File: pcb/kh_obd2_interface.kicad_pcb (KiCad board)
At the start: 2 copper layers, 19 parts, among them J1 OBD2, Q1 CSD18540Q5B, U1 LM74500-Q1, U2 TVS2700DRV, U3 TPSM33620S5QRDNRQ1

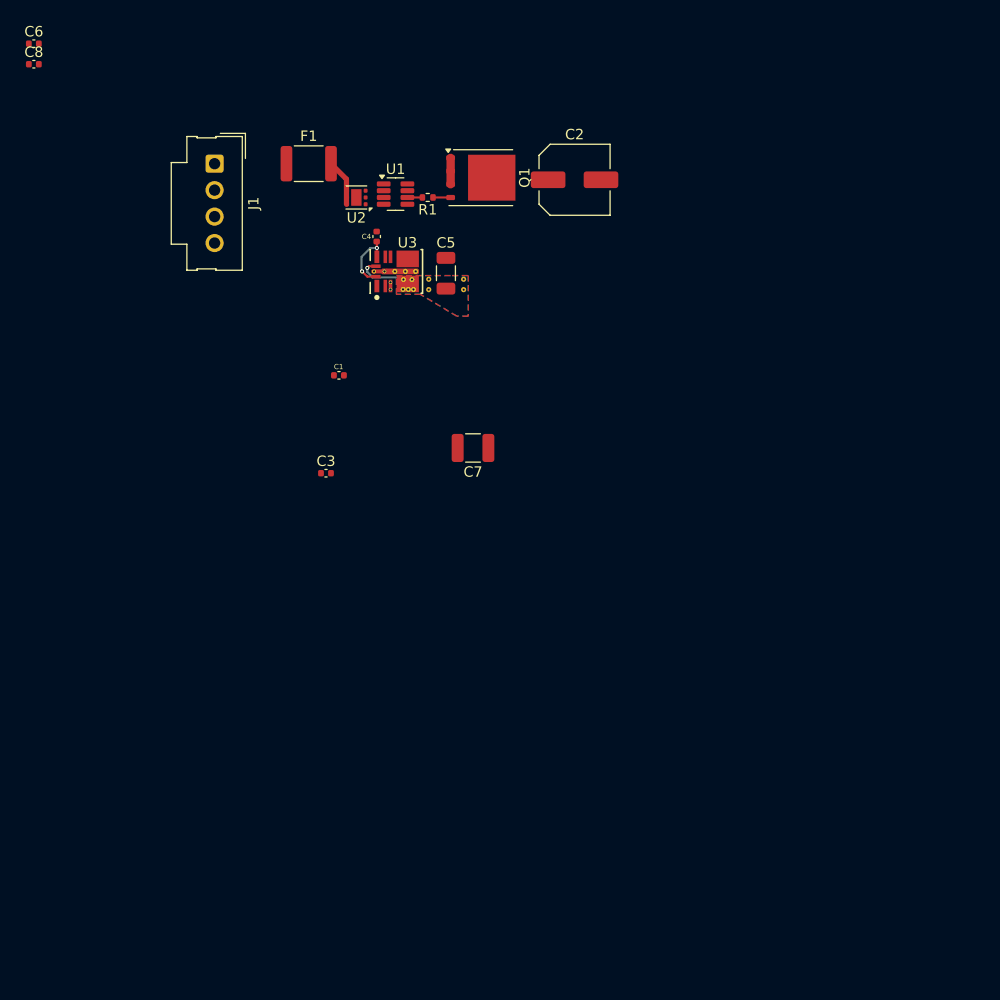
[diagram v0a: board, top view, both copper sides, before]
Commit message: delete old files, fix buck footprint, routing
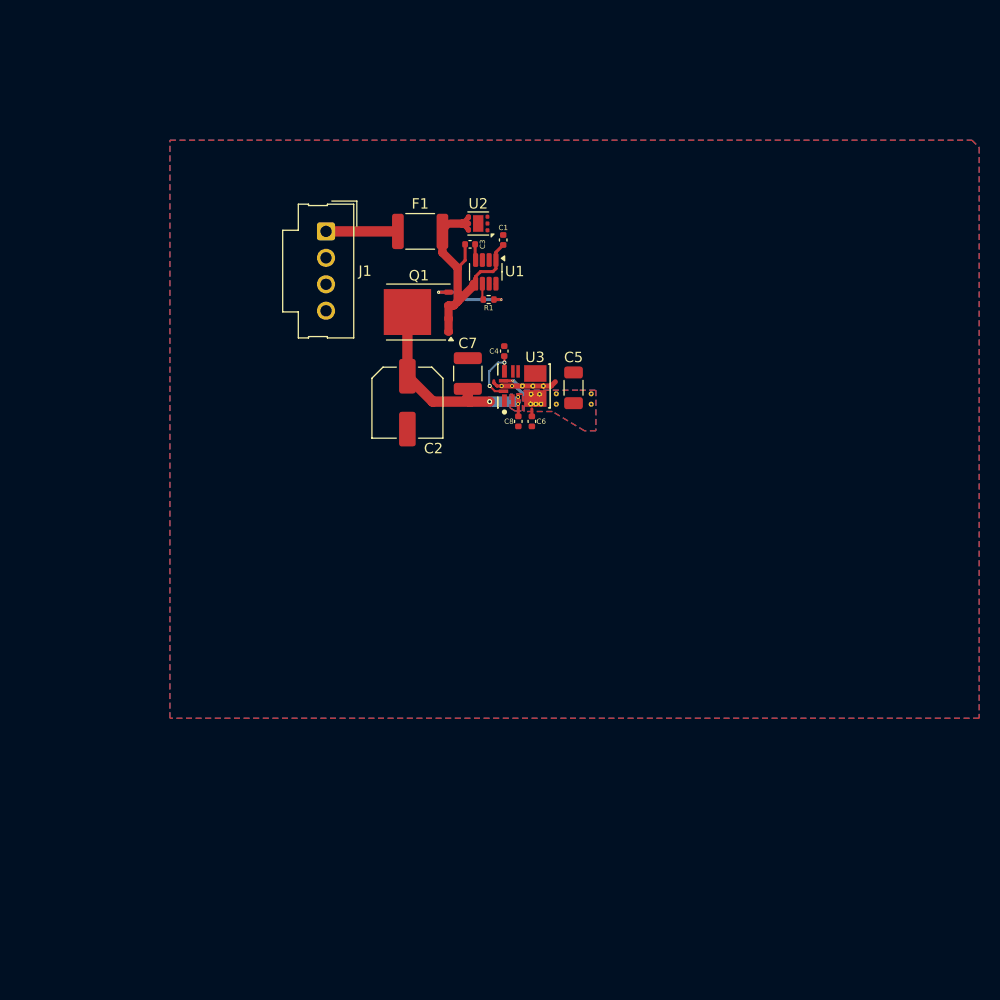
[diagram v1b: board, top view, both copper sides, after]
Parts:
- moved C6 60.0 mm to (48.8, 41.0), turned to 90 degrees
- moved C8 57.8 mm to (47.5, 41.0), turned to 90 degrees
- moved C2 26.8 mm to (36.8, 39.2), turned to -90 degrees
- moved C3 26.0 mm to (42.8, 24.0)
- moved C1 20.4 mm to (46.0, 23.6), turned to 90 degrees
- moved ? 16.5 mm to (54.5, 39.4)
- moved ? 16.5 mm to (51.1, 39.4)
- moved ? 16.5 mm to (54.5, 38.4)
- moved ? 16.5 mm to (51.1, 38.4)
- moved C4 16.5 mm to (46.1, 34.2)
- moved C5 16.5 mm to (52.8, 37.8)
- moved U3 16.5 mm to (48.1, 37.6)
- moved Q1 14.2 mm to (37.9, 30.5), turned to 180 degrees
- moved F1 12.5 mm to (38.0, 22.8)
- moved J1 12.5 mm to (29.0, 22.8)
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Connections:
- U3 pad 5: (no net) -> unconnected-(U3-SW-Pad5)
- U3 pad 6: (no net) -> unconnected-(U3-SW-Pad6)
- U3 pad 7: (no net) -> unconnected-(U3-BOOT-Pad7)
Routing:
- net +12V: track 0.00 -> 20.4 mm, vias 0 -> 1
- net +BATT_FUSED: track 7.05 -> 26.0 mm
- net GND: track 0.00 -> 6.94 mm
- net +BATT: track 0.00 -> 6.90 mm
- net Net-(Q1-G): track 1.69 -> 7.94 mm, vias 0 -> 2
- net Net-(U1-VCAP): track 0.00 -> 1.53 mm
- net +5V: track 5.06 -> 4.39 mm
- added copper zone on B.Cu, net +12V
- added copper zone on F.Cu, net +12V
- added copper zone on B.Cu, net GND
- added copper zone on F.Cu, net GND

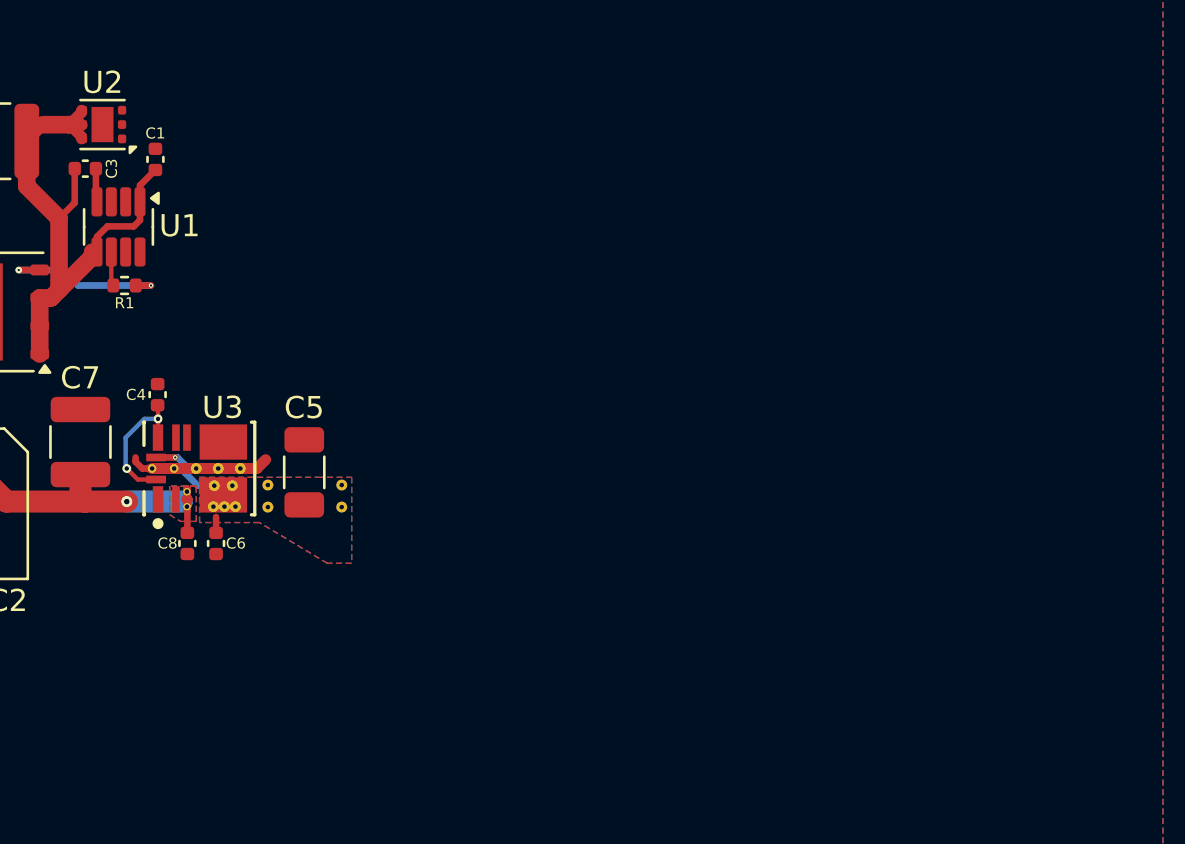
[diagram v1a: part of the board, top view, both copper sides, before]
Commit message: Heirarchal schematics, MCU, more layout
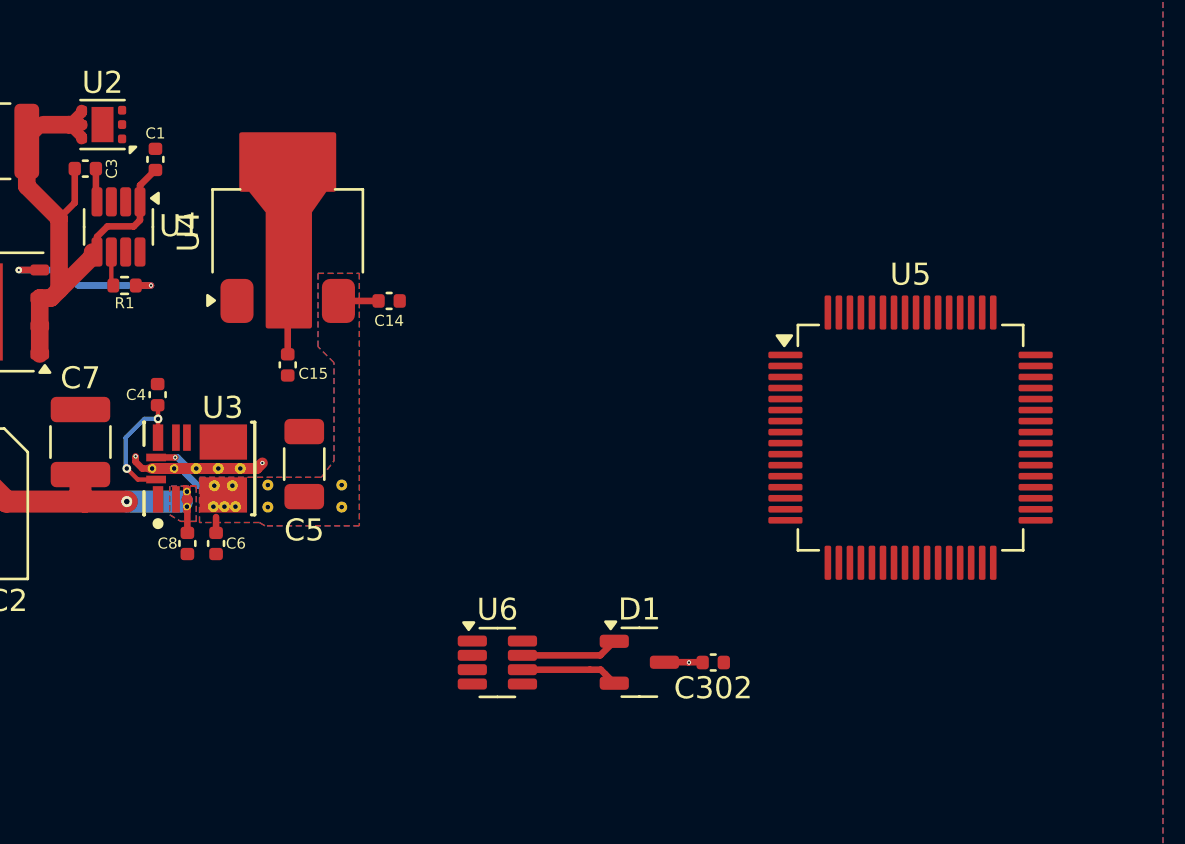
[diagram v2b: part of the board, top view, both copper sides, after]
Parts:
- added C14: 1uF, Capacitor_SMD:C_0402_1005Metric, F.Cu at (56.6, 30.0)
- added C15: 2.2uF, Capacitor_SMD:C_0402_1005Metric, F.Cu at (52.0, 32.9)
- added C302: 4.7nF, Capacitor_SMD:C_0402_1005Metric, F.Cu at (71.3, 46.4)
- added D1: ESD2CANxx24-Q1, Package_TO_SOT_SMD:SOT-23-3, F.Cu at (68.0, 46.4)
- added U4: LM1117-Q1-3.3, Package_TO_SOT_SMD:SOT-223-3_TabPin2, F.Cu at (52.0, 26.9)
- added U5: STM32G0B1RET6, Package_QFP:LQFP-64_10x10mm_P0.5mm, F.Cu at (80.2, 36.2)
- added U6: TCAN3403-Q1, Package_TO_SOT_SMD:TSOT-23-8, F.Cu at (61.5, 46.4)
- moved C5 0.38 mm to (52.8, 37.4)
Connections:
- C1 pad 1: +BATT_FUSED -> /Power/BATT_FUSED
- F1 pad 2: +BATT_FUSED -> /Power/BATT_FUSED
- Q1 pad 1: +BATT_FUSED -> /Power/BATT_FUSED
- Q1 pad 2: +BATT_FUSED -> /Power/BATT_FUSED
- Q1 pad 3: +BATT_FUSED -> /Power/BATT_FUSED
- U1 pad 5: +BATT_FUSED -> /Power/BATT_FUSED
- U2 pad 4: +BATT_FUSED -> /Power/BATT_FUSED
- U2 pad 5: +BATT_FUSED -> /Power/BATT_FUSED
- U2 pad 6: +BATT_FUSED -> /Power/BATT_FUSED
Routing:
- net /Power/BATT_FUSED: track 0.00 -> 26.0 mm
- net +BATT_FUSED: track 26.0 -> 0.00 mm
- net +3.3V: track 0.00 -> 5.12 mm
- net /Transceivers/CAN1.H: track 0.00 -> 4.43 mm
- net /Transceivers/CAN1.L: track 0.00 -> 4.42 mm
- net +5V: track 4.39 -> 6.21 mm
- net GND: track 6.94 -> 8.42 mm, vias 0 -> 3

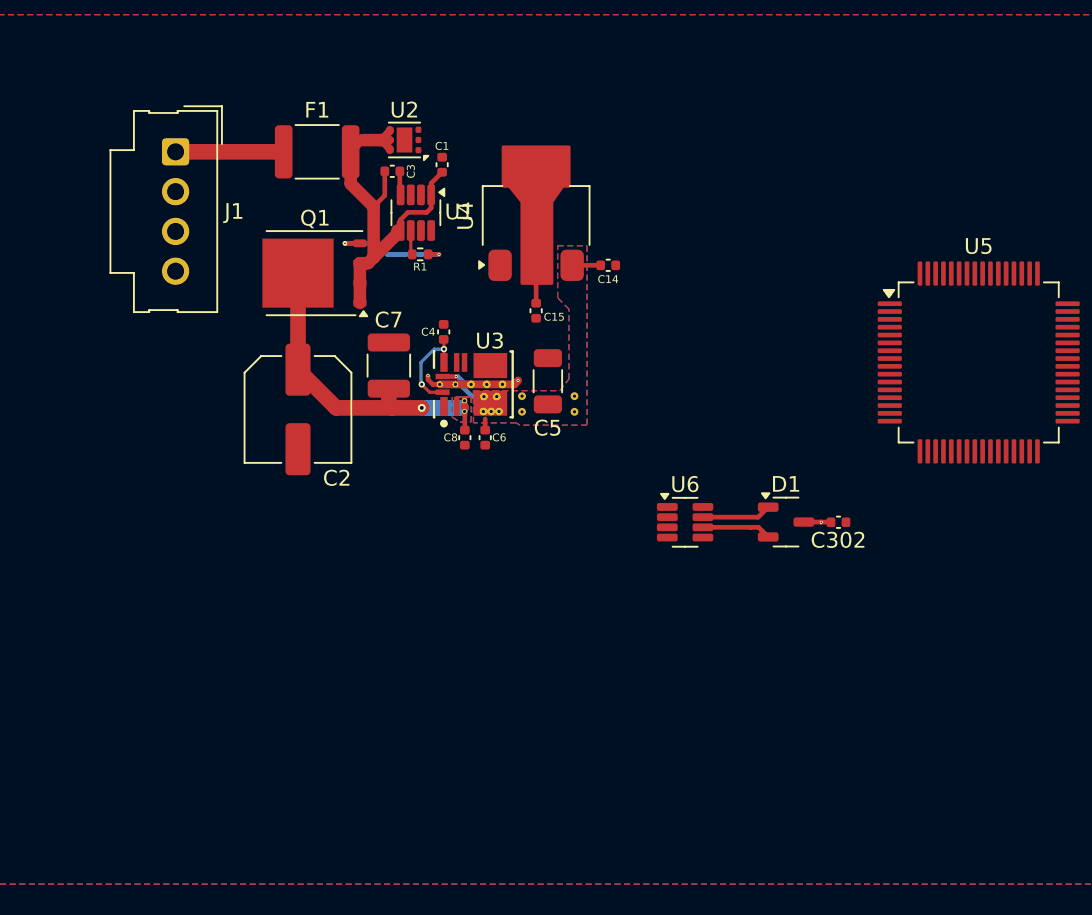
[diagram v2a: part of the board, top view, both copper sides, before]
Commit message: add connectors schem
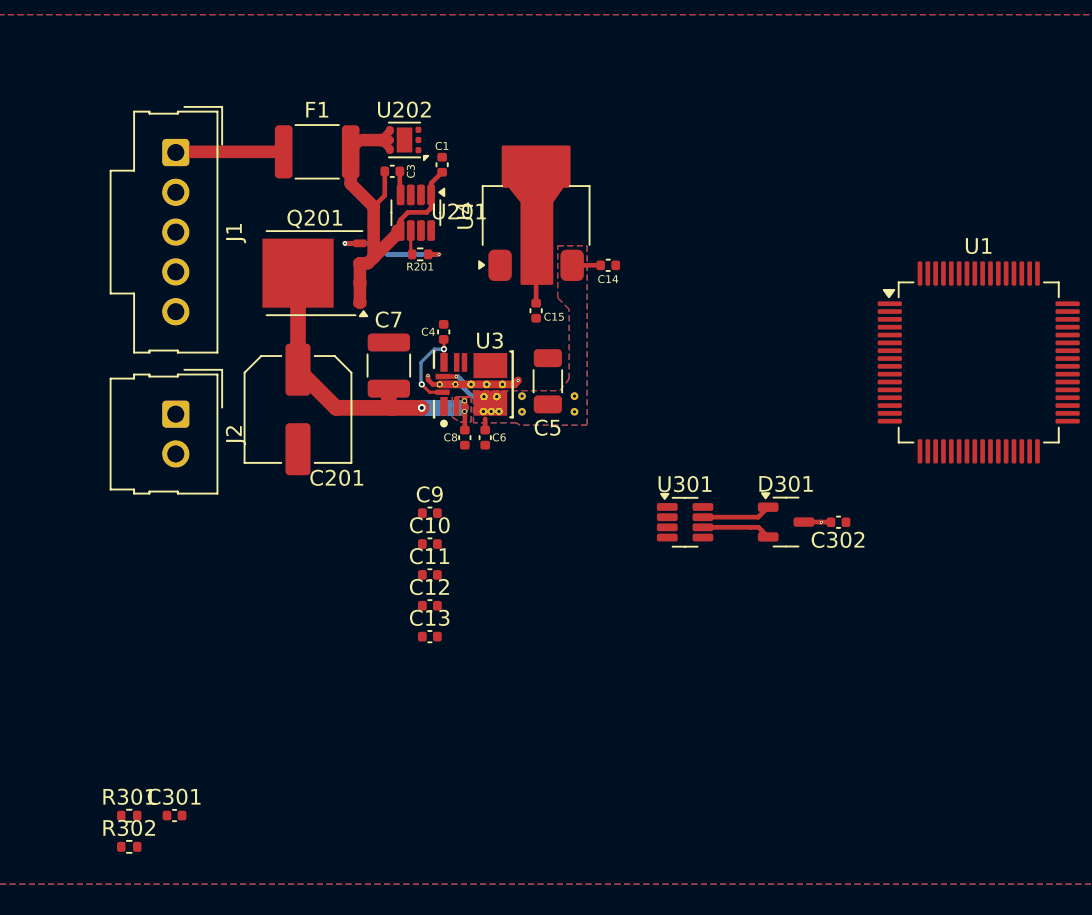
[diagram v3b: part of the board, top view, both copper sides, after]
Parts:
- added C10: 4.7uF, Capacitor_SMD:C_0402_1005Metric, F.Cu at (45.2, 47.8)
- added C11: 100nF, Capacitor_SMD:C_0402_1005Metric, F.Cu at (45.2, 49.8)
- added C12: 1uF, Capacitor_SMD:C_0402_1005Metric, F.Cu at (45.2, 51.7)
- added C13: 100nF, Capacitor_SMD:C_0402_1005Metric, F.Cu at (45.2, 53.7)
- added C301: 1uF, Capacitor_SMD:C_0402_1005Metric, F.Cu at (28.9, 65.1)
- added C9: 100nF, Capacitor_SMD:C_0402_1005Metric, F.Cu at (45.2, 45.8)
- added J2: CAN, Connector_Molex:Molex_SL_171971-0002_1x02_P2.54mm_Vertical, F.Cu at (29.0, 39.5)
- added R301: 60r, Resistor_SMD:R_0402_1005Metric, F.Cu at (26.0, 65.1)
- added R302: 60r, Resistor_SMD:R_0402_1005Metric, F.Cu at (26.0, 67.1)
- J1: footprint Connector_Molex:Molex_SL_171971-0004_1x04_P2.54mm_Vertical -> Connector_Molex:Molex_SL_171971-0005_1x05_P2.54mm_Vertical
- renumbered C2 to C201, D1 to D301, Q1 to Q201, R1 to R201, U5 to U1, U1 to U201, U2 to U202, U6 to U301
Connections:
- net /H Line renamed /Connectors/H Line
- net /K Line renamed /Connectors/K Line
- net /MCU/MCU_BOOT0 renamed /MCU/MCU_SWCLK_BOOT0
- net /SCS renamed /Connectors/SCS
- U1 pad 1: (no net) -> unconnected-(U1-PC11-Pad1)
- U1 pad 10: (no net) -> unconnected-(U1-PF0-Pad10)
- U1 pad 11: (no net) -> unconnected-(U1-PF1-Pad11)
- U1 pad 13: (no net) -> unconnected-(U1-PC0-Pad13)
- U1 pad 14: (no net) -> unconnected-(U1-PC1-Pad14)
- U1 pad 15: (no net) -> unconnected-(U1-PC2-Pad15)
- U1 pad 16: (no net) -> unconnected-(U1-PC3-Pad16)
- U1 pad 17: (no net) -> /MCU/DISPLAY.DC
- U1 pad 18: (no net) -> /MCU/DISPLAY.RST
- U1 pad 19: (no net) -> /MCU/HL_UART.TX
- U1 pad 2: (no net) -> unconnected-(U1-PC12-Pad2)
- U1 pad 20: (no net) -> /MCU/HL_UART.RX
- U1 pad 21: (no net) -> /MCU/DISPLAY.SPI_CS
- U1 pad 22: (no net) -> /MCU/DISPLAY.SPI_CLK
- U1 pad 23: (no net) -> /MCU/DISPLAY.SPI_MISO
- U1 pad 24: (no net) -> /MCU/DISPLAY.SPI_MOSI
- U1 pad 25: (no net) -> /MCU/KL_UART.TX
- U1 pad 26: (no net) -> /MCU/KL_UART.RX
- U1 pad 27: (no net) -> unconnected-(U1-PB0-Pad27)
- U1 pad 28: (no net) -> unconnected-(U1-PB1-Pad28)
- U1 pad 29: (no net) -> unconnected-(U1-PB2-Pad29)
- U1 pad 3: (no net) -> unconnected-(U1-PC13-Pad3)
- U1 pad 32: (no net) -> unconnected-(U1-PB12-Pad32)
- U1 pad 33: (no net) -> unconnected-(U1-PB13-Pad33)
- U1 pad 34: (no net) -> unconnected-(U1-PB14-Pad34)
- U1 pad 35: (no net) -> unconnected-(U1-PB15-Pad35)
- U1 pad 36: (no net) -> unconnected-(U1-PA8-Pad36)
- U1 pad 37: /MCU/KL_UART.TX -> unconnected-(U1-PA9/UCPD1_DBCC1-Pad37)
- U1 pad 38: (no net) -> unconnected-(U1-PC6-Pad38)
- U1 pad 39: (no net) -> unconnected-(U1-PC7-Pad39)
- U1 pad 4: (no net) -> unconnected-(U1-PC14-Pad4)
- U1 pad 40: (no net) -> unconnected-(U1-PD8-Pad40)
- U1 pad 41: (no net) -> unconnected-(U1-PD9-Pad41)
- U1 pad 42: /MCU/KL_UART.RX -> unconnected-(U1-PA10/UCPD1_DBCC2-Pad42)
- U1 pad 45: (no net) -> /MCU/MCU_SWDIO
- U1 pad 47: (no net) -> unconnected-(U1-PA15-Pad47)
- U1 pad 48: (no net) -> unconnected-(U1-PC8-Pad48)
- U1 pad 49: (no net) -> unconnected-(U1-PC9-Pad49)
- U1 pad 5: (no net) -> unconnected-(U1-PC15-Pad5)
- U1 pad 50: (no net) -> unconnected-(U1-PD0-Pad50)
- U1 pad 51: (no net) -> unconnected-(U1-PD1-Pad51)
- U1 pad 52: (no net) -> unconnected-(U1-PD2-Pad52)
- U1 pad 53: (no net) -> unconnected-(U1-PD3-Pad53)
- U1 pad 54: (no net) -> unconnected-(U1-PD4-Pad54)
- U1 pad 55: (no net) -> unconnected-(U1-PD5-Pad55)
- U1 pad 56: (no net) -> unconnected-(U1-PD6-Pad56)
- U1 pad 57: (no net) -> unconnected-(U1-PB3-Pad57)
- U1 pad 58: (no net) -> unconnected-(U1-PB4-Pad58)
- U1 pad 59: (no net) -> unconnected-(U1-PB5-Pad59)
- U1 pad 60: /MCU/HL_UART.TX -> unconnected-(U1-PB6-Pad60)
- U1 pad 61: /MCU/HL_UART.RX -> unconnected-(U1-PB7-Pad61)
- U1 pad 62: (no net) -> unconnected-(U1-PB8-Pad62)
- U1 pad 63: (no net) -> unconnected-(U1-PB9-Pad63)
- U1 pad 64: (no net) -> unconnected-(U1-PC10-Pad64)
- U1 pad 7: /MCU/+3V3 -> +3V3
- U1 pad 8: /MCU/+3V3 -> +3V3
- U301 pad 3: /MCU/+3V3 -> +3.3V
